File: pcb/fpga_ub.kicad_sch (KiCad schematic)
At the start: 9 parts

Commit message: add footprints
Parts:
- U1201: renamed from U?; footprint (none) -> fpga:BGA256C100P16X16_1700X1700X155
- gave numbers to parts that had none: 8
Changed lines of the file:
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@@
   (symbol (lib_id "Connector_Generic:Conn_02x07_Top_Bottom") (at 193.04 69.85 0) (unit 1)
     (in_bom yes) (on_board yes) (fields_autoplaced)
-    (property "Reference" "J?" (id 0) (at 194.31 55.88 0))
+    (property "Reference" "J1201" (id 0) (at 194.31 55.88 0))
     (property "Value" "Conn_02x07_Top_Bottom" (id 1) (at 194.31 58.42 0))
     (property "Footprint" "" (id 2) (at 193.04 69.85 0)
@@
   (symbol (lib_id "Device:C") (at 229.87 25.4 0) (unit 1)
     (in_bom yes) (on_board yes)
-    (property "Reference" "C?" (id 0) (at 230.505 22.86 0)
+    (property "Reference" "C1206" (id 0) (at 230.505 22.86 0)
       (effects (font (size 1.27 1.27)) (justify left))
     )
@@
   (symbol (lib_id "Device:C") (at 185.42 25.4 0) (unit 1)
     (in_bom yes) (on_board yes)
-    (property "Reference" "C?" (id 0) (at 186.055 22.86 0)
+    (property "Reference" "C1201" (id 0) (at 186.055 22.86 0)
       (effects (font (size 1.27 1.27)) (justify left))
     )
@@
   (symbol (lib_id "power:GND") (at 247.65 29.21 0) (unit 1)
     (in_bom yes) (on_board yes)
-    (property "Reference" "#PWR?" (id 0) (at 247.65 35.56 0)
+    (property "Reference" "#PWR01205" (id 0) (at 247.65 35.56 0)
       (effects (font (size 1.27 1.27)) hide)
     )
@@
   (symbol (lib_id "power:+3.3V") (at 200.66 74.93 270) (unit 1)
     (in_bom yes) (on_board yes) (fields_autoplaced)
-    (property "Reference" "#PWR?" (id 0) (at 196.85 74.93 0)
+    (property "Reference" "#PWR01202" (id 0) (at 196.85 74.93 0)
       (effects (font (size 1.27 1.27)) hide)
     )
@@
   (symbol (lib_id "Device:C") (at 238.76 25.4 0) (unit 1)
     (in_bom yes) (on_board yes)
-    (property "Reference" "C?" (id 0) (at 239.395 22.86 0)
+    (property "Reference" "C1207" (id 0) (at 239.395 22.86 0)
       (effects (font (size 1.27 1.27)) (justify left))
     )
@@
   (symbol (lib_id "FPGA_Xilinx_Artix7:XC7A100T-FTG256") (at 93.98 95.25 0) (unit 2)
     (in_bom yes) (on_board yes) (fields_autoplaced)
-    (property "Reference" "U?" (id 0) (at 93.98 171.45 0))
+    (property "Reference" "U1201" (id 0) (at 93.98 171.45 0))
     (property "Value" "XC7A100T-FTG256" (id 1) (at 93.98 173.99 0))
-    (property "Footprint" "" (id 2) (at 93.98 95.25 0)
+    (property "Footprint" "fpga:BGA256C100P16X16_1700X1700X155" (id 2) (at 93.98 95.25 0)
       (effects (font (size 1.27 1.27)) hide)
     )
@@
   (symbol (lib_id "power:+3.3V") (at 247.65 21.59 0) (unit 1)
     (in_bom yes) (on_board yes) (fields_autoplaced)
-    (property "Reference" "#PWR?" (id 0) (at 247.65 25.4 0)
+    (property "Reference" "#PWR01204" (id 0) (at 247.65 25.4 0)
       (effects (font (size 1.27 1.27)) hide)
     )
@@
   (symbol (lib_id "Device:C") (at 219.71 25.4 0) (unit 1)
     (in_bom yes) (on_board yes)
-    (property "Reference" "C?" (id 0) (at 220.345 22.86 0)
+    (property "Reference" "C1205" (id 0) (at 220.345 22.86 0)
       (effects (font (size 1.27 1.27)) (justify left))
     )
@@
   (symbol (lib_id "Device:C") (at 193.04 25.4 0) (unit 1)
     (in_bom yes) (on_board yes)
-    (property "Reference" "C?" (id 0) (at 193.675 22.86 0)
+    (property "Reference" "C1202" (id 0) (at 193.675 22.86 0)
       (effects (font (size 1.27 1.27)) (justify left))
     )
@@
   (symbol (lib_id "power:GND") (at 200.66 77.47 90) (unit 1)
     (in_bom yes) (on_board yes) (fields_autoplaced)
-    (property "Reference" "#PWR?" (id 0) (at 207.01 77.47 0)
+    (property "Reference" "#PWR01203" (id 0) (at 207.01 77.47 0)
       (effects (font (size 1.27 1.27)) hide)
     )
@@
   (symbol (lib_id "power:GND") (at 48.26 21.59 270) (unit 1)
     (in_bom yes) (on_board yes)
-    (property "Reference" "#PWR?" (id 0) (at 41.91 21.59 0)
+    (property "Reference" "#PWR01201" (id 0) (at 41.91 21.59 0)
       (effects (font (size 1.27 1.27)) hide)
     )
@@
   (symbol (lib_id "Device:C") (at 210.82 25.4 0) (unit 1)
     (in_bom yes) (on_board yes)
-    (property "Reference" "C?" (id 0) (at 211.455 22.86 0)
+    (property "Reference" "C1204" (id 0) (at 211.455 22.86 0)
       (effects (font (size 1.27 1.27)) (justify left))
     )
@@
   (symbol (lib_id "Device:C") (at 201.93 25.4 0) (unit 1)
     (in_bom yes) (on_board yes)
-    (property "Reference" "C?" (id 0) (at 202.565 22.86 0)
-      (effects (font (size 1.27 1.27)) (justify left))
-    )
+    (property "Reference" "C1203" (id 0) (at 202.565 22.86 0)
+      (effects (font (size 1.27 1.27)) (justify left))
+    )

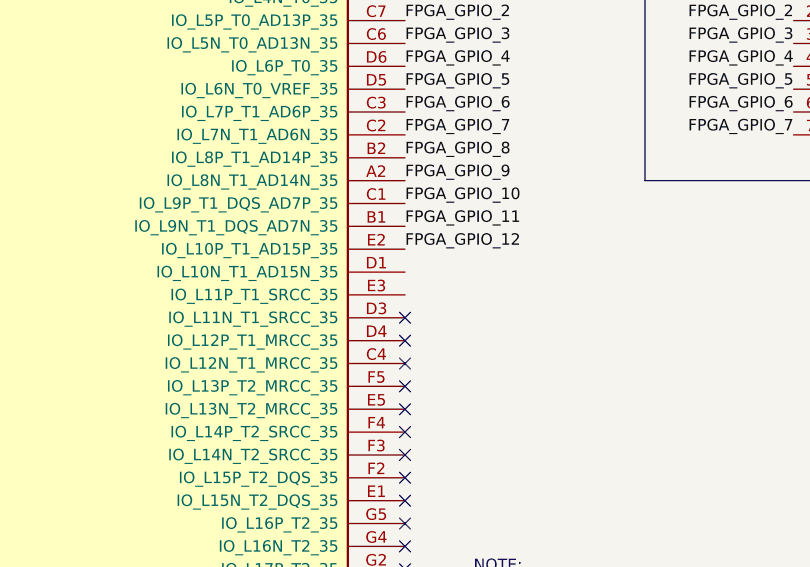
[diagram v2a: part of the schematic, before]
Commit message: add footprints + fix unnconnected
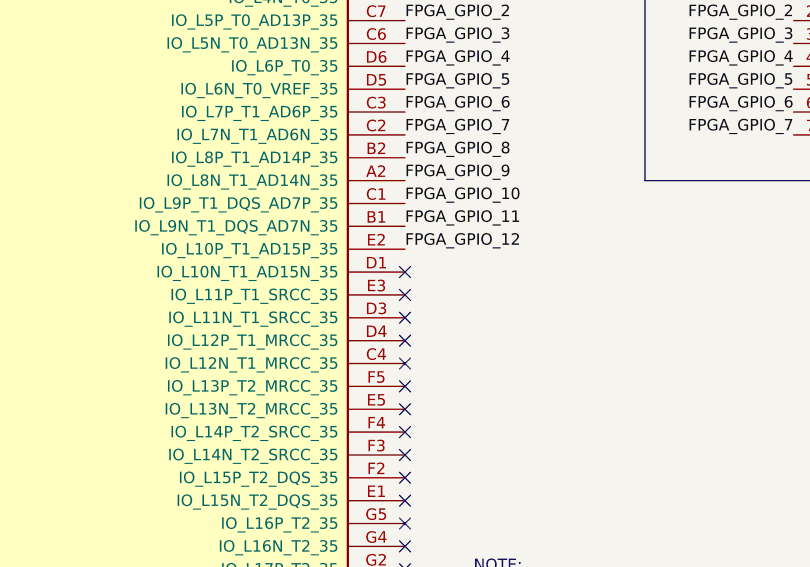
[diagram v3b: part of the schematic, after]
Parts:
- J1201: footprint (none) -> Connector_PinHeader_2.54mm:PinHeader_2x07_P2.54mm_Vertical
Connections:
- no-connect marks 50 -> 52
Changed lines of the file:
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@@
   (no_connect (at 43.18 64.77))
   (no_connect (at 43.18 67.31))
+  (no_connect (at 144.78 92.71))
   (no_connect (at 144.78 57.15))
   (no_connect (at 144.78 59.69))
@@
   (no_connect (at 43.18 54.61))
   (no_connect (at 43.18 57.15))
+  (no_connect (at 144.78 95.25))
   (no_connect (at 144.78 118.11))
   (no_connect (at 144.78 113.03))
@@
     (property "Reference" "J1201" (id 0) (at 194.31 55.88 0))
     (property "Value" "Conn_02x07_Top_Bottom" (id 1) (at 194.31 58.42 0))
-    (property "Footprint" "" (id 2) (at 193.04 69.85 0)
+    (property "Footprint" "Connector_PinHeader_2.54mm:PinHeader_2x07_P2.54mm_Vertical" (id 2) (at 193.04 69.85 0)
       (effects (font (size 1.27 1.27)) hide)
     )

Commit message: start layout
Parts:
- removed U1201: XC7A100T-FTG256, fpga:BGA256C100P16X16_1700X1700X155, symbol FPGA_Xilinx_Artix7:XC7A100T-FTG256
- added U666: XC7A75T-FTG256, Package_BGA:Xilinx_FTG256, symbol FPGA_Xilinx_Artix7:XC7A75T-FTG256
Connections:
- net +3.3V: now also U666.A6 (VCCO_35), U666.B3 (VCCO_35), U666.D7 (VCCO_35), U666.E4 (VCCO_35), U666.F1 (VCCO_35), U666.J2 (VCCO_35)
- net FGPA_MCU_EXTRA1: now also U666.B5 (IO_L2N_T0_AD12N_35)
- net FGPA_MCU_EXTRA2: now also U666.A5 (IO_L3P_T0_DQS_AD5P_35)
- net FGPA_MCU_SPI_CLK: now also U666.E6 (IO_0_35)
- net FGPA_MCU_SPI_CS: now also U666.B7 (IO_L1P_T0_AD4P_35)
- net FGPA_MCU_SPI_SDI: now also U666.A7 (IO_L1N_T0_AD4N_35)
- net FGPA_MCU_SPI_SDO: now also U666.B6 (IO_L2P_T0_AD12P_35)
- net FPGA_DEBUG_LED_BLOCK35_1: now also U666.H5 (IO_L18P_T2_35)
- net FPGA_DEBUG_LED_BLOCK35_2: now also U666.J5 (IO_L19P_T3_35)
- net FPGA_GPIO_1: now also U666.A3 (IO_L4N_T0_35)
- net FPGA_GPIO_10: now also U666.C1 (IO_L9P_T1_DQS_AD7P_35)
- net FPGA_GPIO_11: now also U666.B1 (IO_L9N_T1_DQS_AD7N_35)
- net FPGA_GPIO_12: now also U666.E2 (IO_L10P_T1_AD15P_35)
- net FPGA_GPIO_2: now also U666.C7 (IO_L5P_T0_AD13P_35)
- net FPGA_GPIO_3: now also U666.C6 (IO_L5N_T0_AD13N_35)
- net FPGA_GPIO_4: now also U666.D6 (IO_L6P_T0_35)
- net FPGA_GPIO_5: now also U666.D5 (IO_L6N_T0_VREF_35)
- net FPGA_GPIO_6: now also U666.C3 (IO_L7P_T1_AD6P_35)
- net FPGA_GPIO_7: now also U666.C2 (IO_L7N_T1_AD6N_35)
- net FPGA_GPIO_8: now also U666.B2 (IO_L8P_T1_AD14P_35)
- net FPGA_GPIO_9: now also U666.A2 (IO_L8N_T1_AD14N_35)
- net GND: now also U666.M3 (VCCO_34), U666.R4 (VCCO_34), U666.T1 (VCCO_34)
- no-connect marks 52 -> 50

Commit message: workon
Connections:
- net FGPA_MCU_SPI_CLK: now also U666.B4 (IO_L4P_T0_35); no longer U666.E6 (IO_0_35)
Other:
- note added: "flyttet spi pin fra e6 til b4"
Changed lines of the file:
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@@
   (no_connect (at 43.18 67.31))
   (no_connect (at 144.78 92.71))
+  (no_connect (at 144.78 41.91))
   (no_connect (at 144.78 57.15))
-  (no_connect (at 144.78 59.69))
   (no_connect (at 43.18 41.91))
   (no_connect (at 43.18 44.45))
@@
     (effects (font (size 1.27 1.27)) (justify left bottom))
   )
+  (text "flyttet spi pin fra e6 til b4\n" (at 147.32 38.1 0)
+    (effects (font (size 1.27 1.27)) (justify left bottom))
+  )
   (label "FPGA_GPIO_2" (at 144.78 64.77 0)
     (effects (font (size 1.27 1.27)) (justify left bottom))
@@
     )
   )
+  (global_label "FGPA_MCU_SPI_CLK" (shape input) (at 144.78 59.69 0) (fields_autoplaced)
+    (effects (font (size 1.27 1.27)) (justify left))
+    (property "Intersheet References" "${INTERSHEET_REFS}" (id 0) (at 165.5174 59.6106 0)
+      (effects (font (size 1.27 1.27)) (justify left) hide)
+    )
+  )
   (global_label "FPGA_DEBUG_LED_BLOCK35_1" (shape input) (at 151.13 130.81 0) (fields_autoplaced)
     (effects (font (size 1.27 1.27)) (justify left))
@@
       (effects (font (size 1.27 1.27)) (justify left) hide)
     )
-  )
-  (global_label "FGPA_MCU_SPI_CLK" (shape input) (at 144.78 41.91 0) (fields_autoplaced)
-    (effects (font (size 1.27 1.27)) (justify left))
-    (property "Intersheet References" "${INTERSHEET_REFS}" (id 0) (at 165.5174 41.8306 0)
-      (effects (font (size 1.27 1.27)) (justify left) hide)
-    )

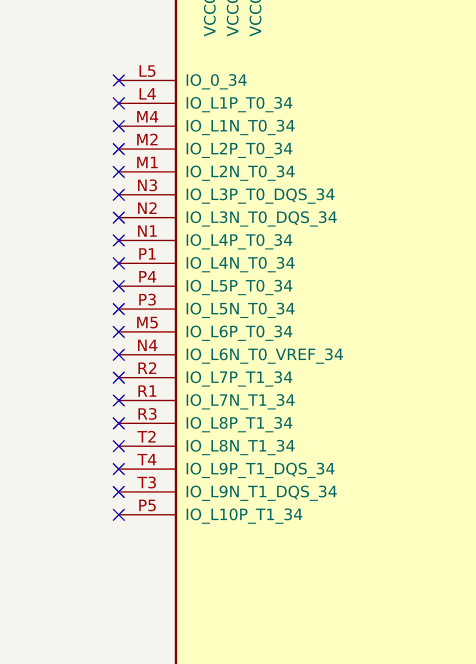
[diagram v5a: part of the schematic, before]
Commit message: make lines between sram and fpga
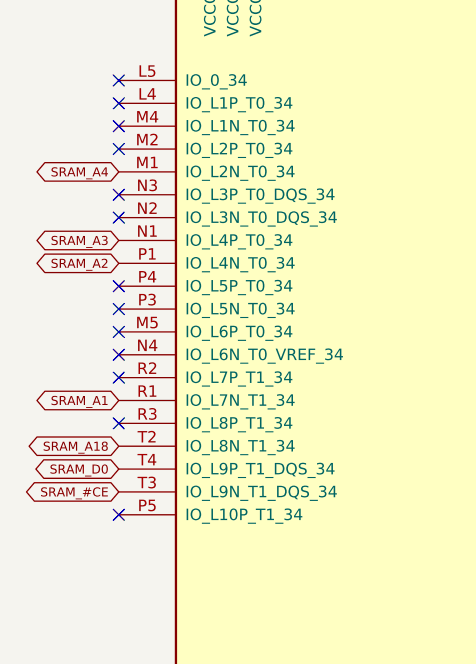
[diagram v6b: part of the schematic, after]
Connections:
- net SRAM_A4: now reaches U666.M1 (IO_L2N_T0_34)
- net SRAM_A3: now reaches U666.N1 (IO_L4P_T0_34)
- net SRAM_A2: now reaches U666.P1 (IO_L4N_T0_34)
- net SRAM_A1: now reaches U666.R1 (IO_L7N_T1_34)
- net SRAM_A18: now reaches U666.T2 (IO_L8N_T1_34)
- net SRAM_#CE: now reaches U666.T3 (IO_L9N_T1_DQS_34)
- net SRAM_D0: now reaches U666.T4 (IO_L9P_T1_DQS_34)
- no-connect marks 50 -> 43
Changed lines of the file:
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@@
   (no_connect (at 43.18 46.99))
   (no_connect (at 43.18 49.53))
-  (no_connect (at 43.18 52.07))
   (no_connect (at 43.18 54.61))
   (no_connect (at 43.18 57.15))
@@
   (no_connect (at 43.18 72.39))
   (no_connect (at 43.18 74.93))
-  (no_connect (at 43.18 77.47))
   (no_connect (at 43.18 80.01))
-  (no_connect (at 43.18 82.55))
-  (no_connect (at 43.18 85.09))
-  (no_connect (at 43.18 87.63))
   (no_connect (at 43.18 90.17))
   (no_connect (at 144.78 120.65))
@@
   (no_connect (at 144.78 163.83))
   (no_connect (at 144.78 166.37))
-  (no_connect (at 43.18 59.69))
-  (no_connect (at 43.18 62.23))
   (no_connect (at 144.78 110.49))
   (wire (pts (xy 193.04 29.21) (xy 201.93 29.21))
@@
     (effects (font (size 1.27 1.27)) (justify left bottom))
   )
+  (global_label "SRAM_A3" (shape bidirectional) (at 43.18 59.69 180) (fields_autoplaced)
+    (effects (font (size 1 1)) (justify right))
+    (property "Intersheet References" "${INTERSHEET_REFS}" (id 0) (at 34.7562 59.6275 0)
+      (effects (font (size 1 1)) (justify right) hide)
+    )
+  )
+  (global_label "SRAM_A18" (shape bidirectional) (at 43.18 82.55 180) (fields_autoplaced)
+    (effects (font (size 1 1)) (justify right))
+    (property "Intersheet References" "${INTERSHEET_REFS}" (id 0) (at 33.8038 82.4875 0)
+      (effects (font (size 1 1)) (justify right) hide)
+    )
+  )
   (global_label "FPGA_DEBUG_LED_BLOCK35_2" (shape input) (at 151.13 135.89 0) (fields_autoplaced)
     (effects (font (size 1.27 1.27)) (justify left))
@@
     )
   )
+  (global_label "SRAM_A2" (shape bidirectional) (at 43.18 62.23 180) (fields_autoplaced)
+    (effects (font (size 1 1)) (justify right))
+    (property "Intersheet References" "${INTERSHEET_REFS}" (id 0) (at 34.7562 62.1675 0)
+      (effects (font (size 1 1)) (justify right) hide)
+    )
+  )
   (global_label "FGPA_MCU_SPI_SDI" (shape input) (at 144.78 46.99 0) (fields_autoplaced)
     (effects (font (size 1.27 1.27)) (justify left))
@@
     )
   )
+  (global_label "SRAM_A1" (shape bidirectional) (at 43.18 77.47 180) (fields_autoplaced)
+    (effects (font (size 1 1)) (justify right))
+    (property "Intersheet References" "${INTERSHEET_REFS}" (id 0) (at 34.7562 77.4075 0)
+      (effects (font (size 1 1)) (justify right) hide)
+    )
+  )
   (global_label "FPGA_DEBUG_LED_BLOCK35_1" (shape input) (at 151.13 130.81 0) (fields_autoplaced)
     (effects (font (size 1.27 1.27)) (justify left))
@@
     )
   )
+  (global_label "SRAM_A4" (shape bidirectional) (at 43.18 52.07 180) (fields_autoplaced)
+    (effects (font (size 1 1)) (justify right))
+    (property "Intersheet References" "${INTERSHEET_REFS}" (id 0) (at 34.7562 52.0075 0)
+      (effects (font (size 1 1)) (justify right) hide)
+    )
+  )
+  (global_label "SRAM_#CE" (shape bidirectional) (at 43.18 87.63 180) (fields_autoplaced)
+    (effects (font (size 1 1)) (justify right))
+    (property "Intersheet References" "${INTERSHEET_REFS}" (id 0) (at 33.661 87.5675 0)
+      (effects (font (size 1 1)) (justify right) hide)
+    )
+  )
   (global_label "FGPA_MCU_SPI_SDO" (shape output) (at 144.78 49.53 0) (fields_autoplaced)
     (effects (font (size 1.27 1.27)) (justify left))
@@
     )
   )
+  (global_label "SRAM_D0" (shape bidirectional) (at 43.18 85.09 180) (fields_autoplaced)
+    (effects (font (size 1 1)) (justify right))
+    (property "Intersheet References" "${INTERSHEET_REFS}" (id 0) (at 34.6133 85.0275 0)
+      (effects (font (size 1 1)) (justify right) hide)
+    )
+  )

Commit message: vga is live
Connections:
- net FGPA_MCU_EXTRA1: now also U666.F2 (IO_L15P_T2_DQS_35); no longer U666.B5 (IO_L2N_T0_AD12N_35)
- net FGPA_MCU_SPI_CLK: now also U666.H2 (IO_L20P_T3_35); no longer U666.B4 (IO_L4P_T0_35)
- net FGPA_MCU_SPI_CS: now also U666.G1 (IO_L17N_T2_35); no longer U666.B7 (IO_L1P_T0_AD4P_35)
- net FGPA_MCU_SPI_SDI: now also U666.G2 (IO_L17P_T2_35); no longer U666.A7 (IO_L1N_T0_AD4N_35)
- net FGPA_MCU_SPI_SDO: now also U666.H1 (IO_L20N_T3_35); no longer U666.B6 (IO_L2P_T0_AD12P_35)
- net FPGA_GPIO_1: no longer U666.A3 (IO_L4N_T0_35)
- net FPGA_GPIO_10: no longer U666.C1 (IO_L9P_T1_DQS_AD7P_35)
- net FPGA_GPIO_11: no longer U666.B1 (IO_L9N_T1_DQS_AD7N_35)
- net FPGA_GPIO_7: no longer U666.C2 (IO_L7N_T1_AD6N_35)
- net FPGA_GPIO_8: no longer U666.B2 (IO_L8P_T1_AD14P_35)
- net FPGA_GPIO_9: no longer U666.A2 (IO_L8N_T1_AD14N_35)
- net vga_r5: now reaches U666.A4 (IO_L3N_T0_DQS_AD5N_35)
- net FGPA_MCU_EXTRA2 renamed vga_g5
- new net vga_g1: U666.B7 (IO_L1P_T0_AD4P_35)
- new net vga_g2: U666.A7 (IO_L1N_T0_AD4N_35)
- new net vga_g3: U666.B6 (IO_L2P_T0_AD12P_35)
- new net vga_g4: U666.B5 (IO_L2N_T0_AD12N_35)
- new net vga_g6: U666.B4 (IO_L4P_T0_35)
- new net vga_r1: U666.B1 (IO_L9N_T1_DQS_AD7N_35)
- new net vga_r2: U666.A2 (IO_L8N_T1_AD14N_35)
- new net vga_r3: U666.B2 (IO_L8P_T1_AD14P_35)
- new net vga_r4: U666.A3 (IO_L4N_T0_35)
- no-connect marks 43 -> 39
